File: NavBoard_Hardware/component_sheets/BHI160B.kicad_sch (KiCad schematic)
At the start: 12 parts

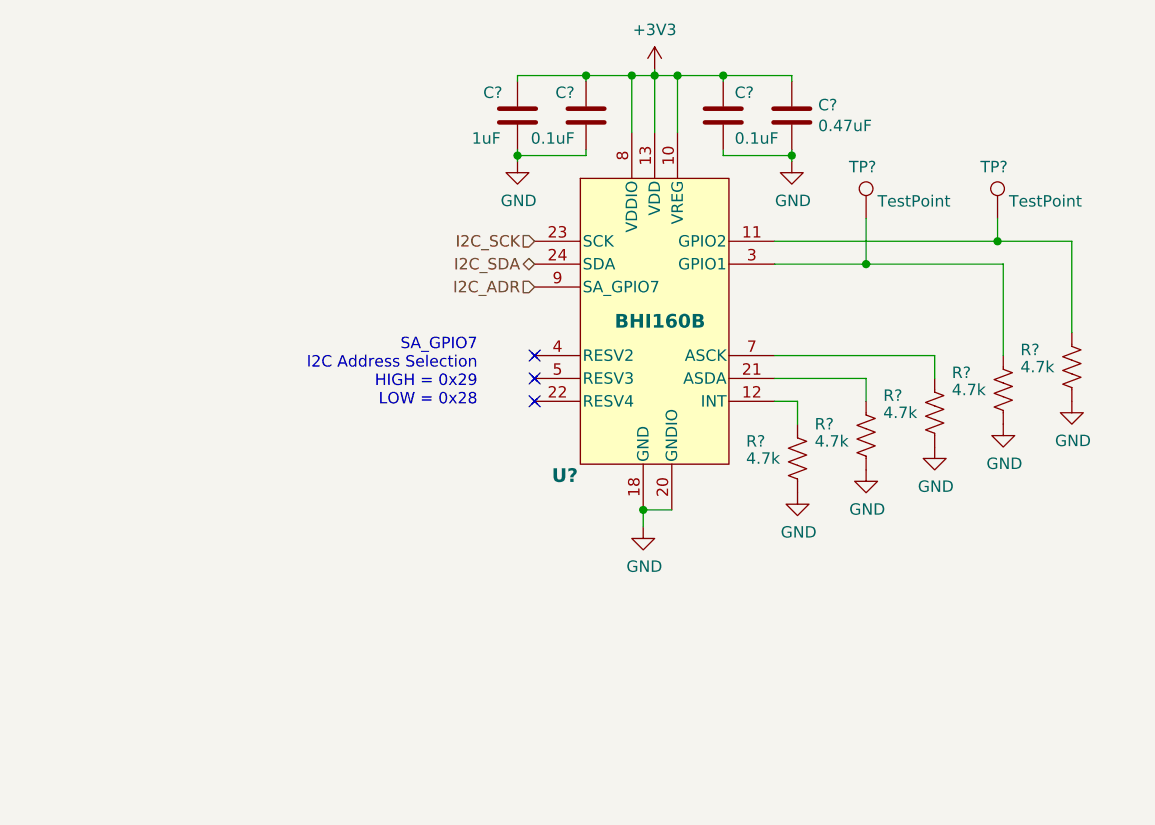
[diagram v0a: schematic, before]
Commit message: Created adapter symbols and footprints
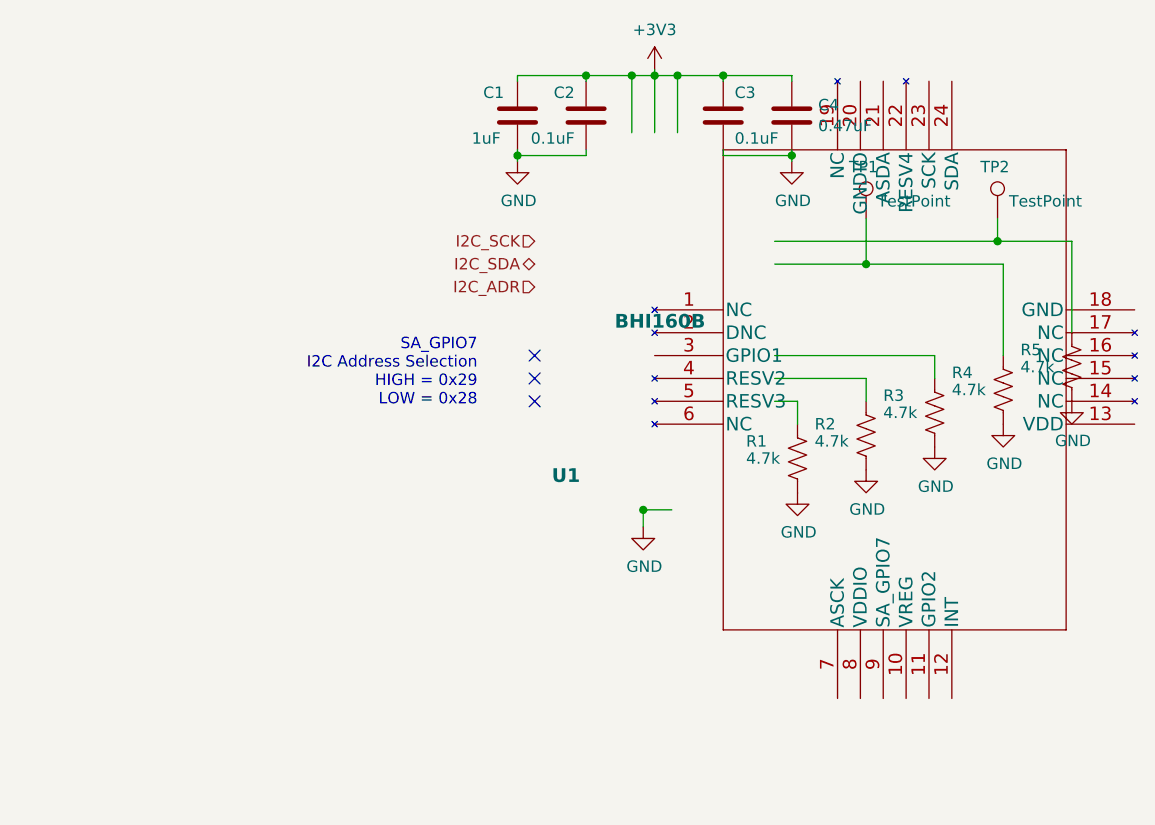
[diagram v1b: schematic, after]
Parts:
- gave numbers to parts that had none: 12
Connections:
- net +3V3: no longer U1.10 (VREG), U1.13 (VDD), U1.8 (VDDIO)
- net GND: no longer U1.18 (GND), U1.20 (GNDIO)
- net I2C_ADR: no longer U1.9 (SA_GPIO7)
- net I2C_SCK: no longer U1.23 (SCK)
- net I2C_SDA: no longer U1.24 (SDA)
- net at R4.1, TP1.1: no longer U1.3 (GPIO1)
- net at R3.1: no longer U1.7 (ASCK)
- net at R5.1, TP2.1: no longer U1.11 (GPIO2)
- net at U1.12 (INT): no longer R1.1
- net at U1.21 (ASDA): no longer R2.1
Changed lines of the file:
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@@
   (symbol (lib_id "Device:R_US") (at 216.535 80.645 0) (unit 1)
     (in_bom yes) (on_board yes)
-    (property "Reference" "R?" (id 0) (at 210.82 78.74 0)
+    (property "Reference" "R4" (id 0) (at 210.82 78.74 0)
       (effects (font (size 1.27 1.27)) (justify left))
     )
@@
   (symbol (lib_id "Device:R_US") (at 208.915 83.185 0) (unit 1)
     (in_bom yes) (on_board yes)
-    (property "Reference" "R?" (id 0) (at 203.2 81.28 0)
+    (property "Reference" "R3" (id 0) (at 203.2 81.28 0)
       (effects (font (size 1.27 1.27)) (justify left))
     )
@@
   (symbol (lib_id "power:GND") (at 176.53 95.885 0) (unit 1)
     (in_bom yes) (on_board yes)
-    (property "Reference" "#PWR?" (id 0) (at 176.53 102.235 0)
+    (property "Reference" "#PWR02" (id 0) (at 176.53 102.235 0)
       (effects (font (size 1.27 1.27)) hide)
     )
@@
   (symbol (lib_id "power:GND") (at 201.295 89.535 0) (unit 1)
     (in_bom yes) (on_board yes)
-    (property "Reference" "#PWR?" (id 0) (at 201.295 95.885 0)
+    (property "Reference" "#PWR06" (id 0) (at 201.295 95.885 0)
       (effects (font (size 1.27 1.27)) hide)
     )
@@
   (symbol (lib_id "Device:R_US") (at 224.155 78.105 0) (unit 1)
     (in_bom yes) (on_board yes)
-    (property "Reference" "R?" (id 0) (at 218.44 76.2 0)
+    (property "Reference" "R5" (id 0) (at 218.44 76.2 0)
       (effects (font (size 1.27 1.27)) (justify left))
     )
@@
   (symbol (lib_id "power:GND") (at 162.56 55.245 0) (unit 1)
     (in_bom yes) (on_board yes)
-    (property "Reference" "#PWR?" (id 0) (at 162.56 61.595 0)
+    (property "Reference" "#PWR01" (id 0) (at 162.56 61.595 0)
       (effects (font (size 1.27 1.27)) hide)
     )
@@
   (symbol (lib_id "power:GND") (at 193.04 55.245 0) (unit 1)
     (in_bom yes) (on_board yes)
-    (property "Reference" "#PWR?" (id 0) (at 193.04 61.595 0)
+    (property "Reference" "#PWR04" (id 0) (at 193.04 61.595 0)
       (effects (font (size 1.27 1.27)) hide)
     )
@@
   (symbol (lib_id "power:GND") (at 216.535 84.455 0) (unit 1)
     (in_bom yes) (on_board yes)
-    (property "Reference" "#PWR?" (id 0) (at 216.535 90.805 0)
+    (property "Reference" "#PWR08" (id 0) (at 216.535 90.805 0)
       (effects (font (size 1.27 1.27)) hide)
     )
@@
   (symbol (lib_id "Device:C") (at 193.04 50.165 0) (unit 1)
     (in_bom yes) (on_board yes)
-    (property "Reference" "C?" (id 0) (at 195.961 48.9966 0)
+    (property "Reference" "C4" (id 0) (at 195.961 48.9966 0)
       (effects (font (size 1.27 1.27)) (justify left))
     )
@@
   (symbol (lib_id "MRDT_Sensors:BHI160B") (at 177.8 71.755 0) (unit 1)
     (in_bom yes) (on_board yes)
-    (property "Reference" "U?" (id 0) (at 166.37 90.17 0)
+    (property "Reference" "U1" (id 0) (at 166.37 90.17 0)
       (effects (font (size 1.524 1.524) bold) (justify left))
     )
@@
       (effects (font (size 1.524 1.524)) hide)
     )
+    (pin "1")
     (pin "10")
     (pin "11")
     (pin "12")
     (pin "13")
+    (pin "14")
+    (pin "15")
+    (pin "16")
+    (pin "17")
     (pin "18")
+    (pin "19")
+    (pin "2")
     (pin "20")
     (pin "21")
@@
     (pin "4")
     (pin "5")
+    (pin "6")
     (pin "7")
     (pin "8")
@@
   (symbol (lib_id "Device:R_US") (at 193.675 88.265 0) (unit 1)
     (in_bom yes) (on_board yes)
-    (property "Reference" "R?" (id 0) (at 187.96 86.36 0)
+    (property "Reference" "R1" (id 0) (at 187.96 86.36 0)
       (effects (font (size 1.27 1.27)) (justify left))
     )
@@
   (symbol (lib_id "power:+3V3") (at 177.8 45.085 0) (unit 1)
     (in_bom yes) (on_board yes)
-    (property "Reference" "#PWR?" (id 0) (at 177.8 48.895 0)
+    (property "Reference" "#PWR03" (id 0) (at 177.8 48.895 0)
       (effects (font (size 1.27 1.27)) hide)
     )
@@
   (symbol (lib_id "Connector:TestPoint") (at 215.9 61.595 0) (unit 1)
     (in_bom yes) (on_board yes)
-    (property "Reference" "TP?" (id 0) (at 213.995 55.88 0)
+    (property "Reference" "TP2" (id 0) (at 213.995 55.88 0)
       (effects (font (size 1.27 1.27)) (justify left))
     )
@@
   (symbol (lib_id "power:GND") (at 224.155 81.915 0) (unit 1)
     (in_bom yes) (on_board yes)
-    (property "Reference" "#PWR?" (id 0) (at 224.155 88.265 0)
+    (property "Reference" "#PWR09" (id 0) (at 224.155 88.265 0)
       (effects (font (size 1.27 1.27)) hide)
     )
@@
   (symbol (lib_id "Device:C") (at 170.18 50.165 0) (mirror y) (unit 1)
     (in_bom yes) (on_board yes)
-    (property "Reference" "C?" (id 0) (at 168.91 47.625 0)
+    (property "Reference" "C2" (id 0) (at 168.91 47.625 0)
       (effects (font (size 1.27 1.27)) (justify left))
     )
@@
   (symbol (lib_id "power:GND") (at 208.915 86.995 0) (unit 1)
     (in_bom yes) (on_board yes)
-    (property "Reference" "#PWR?" (id 0) (at 208.915 93.345 0)
+    (property "Reference" "#PWR07" (id 0) (at 208.915 93.345 0)
       (effects (font (size 1.27 1.27)) hide)
     )
@@
   (symbol (lib_id "Device:C") (at 185.42 50.165 0) (unit 1)
     (in_bom yes) (on_board yes)
-    (property "Reference" "C?" (id 0) (at 186.69 47.625 0)
+    (property "Reference" "C3" (id 0) (at 186.69 47.625 0)
       (effects (font (size 1.27 1.27)) (justify left))
     )
@@
   (symbol (lib_id "Device:R_US") (at 201.295 85.725 0) (unit 1)
     (in_bom yes) (on_board yes)
-    (property "Reference" "R?" (id 0) (at 195.58 84.455 0)
+    (property "Reference" "R2" (id 0) (at 195.58 84.455 0)
       (effects (font (size 1.27 1.27)) (justify left))
     )
@@
   (symbol (lib_id "Device:C") (at 162.56 50.165 0) (unit 1)
     (in_bom yes) (on_board yes)
-    (property "Reference" "C?" (id 0) (at 158.75 47.625 0)
+    (property "Reference" "C1" (id 0) (at 158.75 47.625 0)
       (effects (font (size 1.27 1.27)) (justify left))
     )
@@
   (symbol (lib_id "power:GND") (at 193.675 92.075 0) (unit 1)
     (in_bom yes) (on_board yes)
-    (property "Reference" "#PWR?" (id 0) (at 193.675 98.425 0)
+    (property "Reference" "#PWR05" (id 0) (at 193.675 98.425 0)
       (effects (font (size 1.27 1.27)) hide)
     )
@@
   (symbol (lib_id "Connector:TestPoint") (at 201.295 61.595 0) (unit 1)
     (in_bom yes) (on_board yes)
-    (property "Reference" "TP?" (id 0) (at 199.39 55.88 0)
-      (effects (font (size 1.27 1.27)) (justify left))
-    )
+    (property "Reference" "TP1" (id 0) (at 199.39 55.88 0)
+      (effects (font (size 1.27 1.27)) (justify left))
+    )

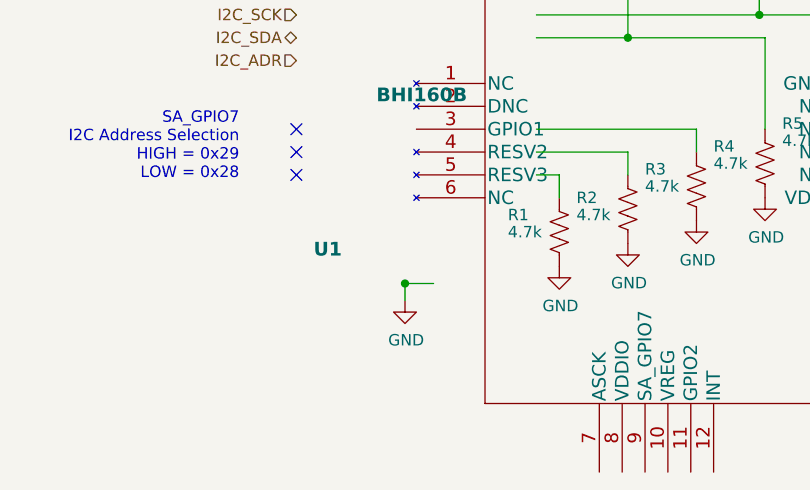
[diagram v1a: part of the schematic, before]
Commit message: Added connectors, cleaned up file directory
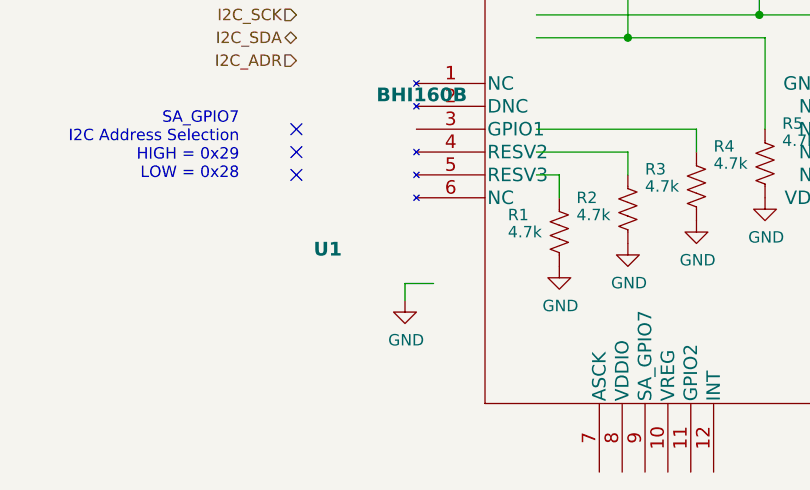
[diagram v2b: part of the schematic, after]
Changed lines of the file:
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@@
   (junction (at 162.56 54.61) (diameter 0) (color 0 0 0 0)
-  )
-  (junction (at 176.53 93.98) (diameter 0) (color 0 0 0 0)
   )
   (junction (at 170.18 45.72) (diameter 0) (color 0 0 0 0)

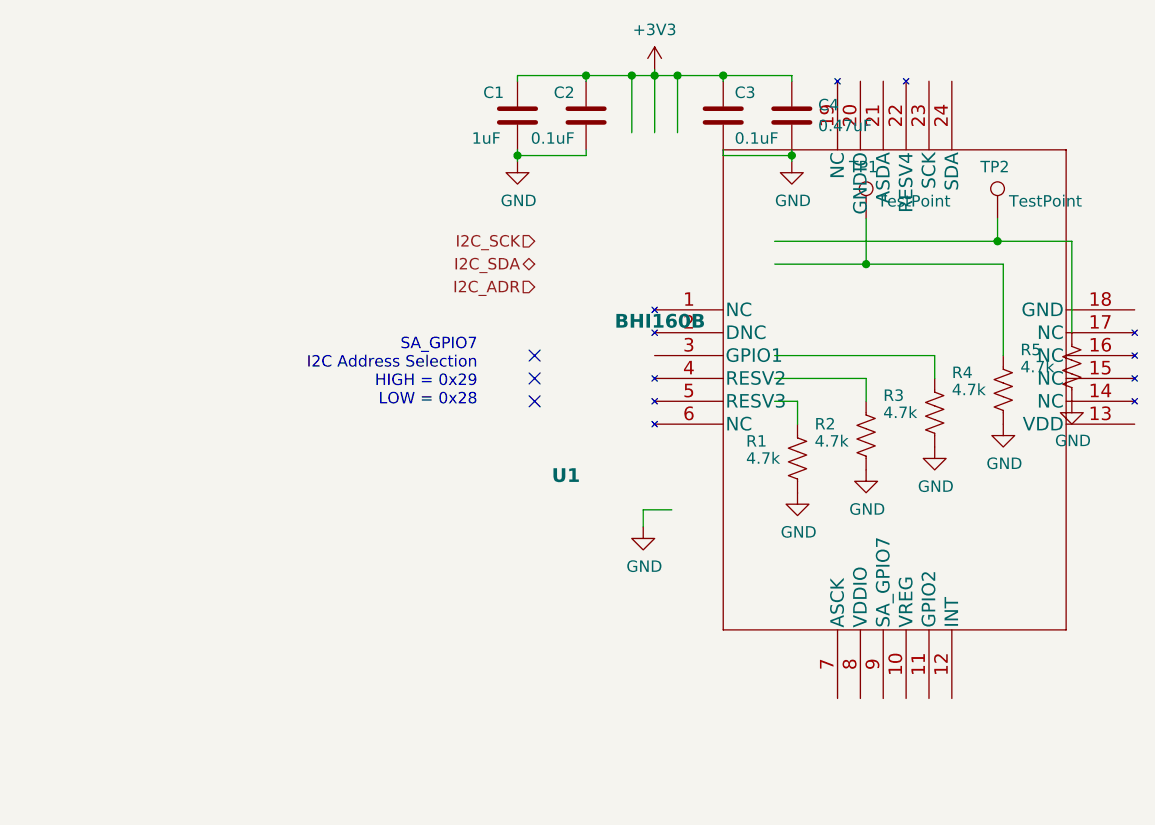
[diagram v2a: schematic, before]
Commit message: Updated BMI component sheet from Navboard_2023_rev2
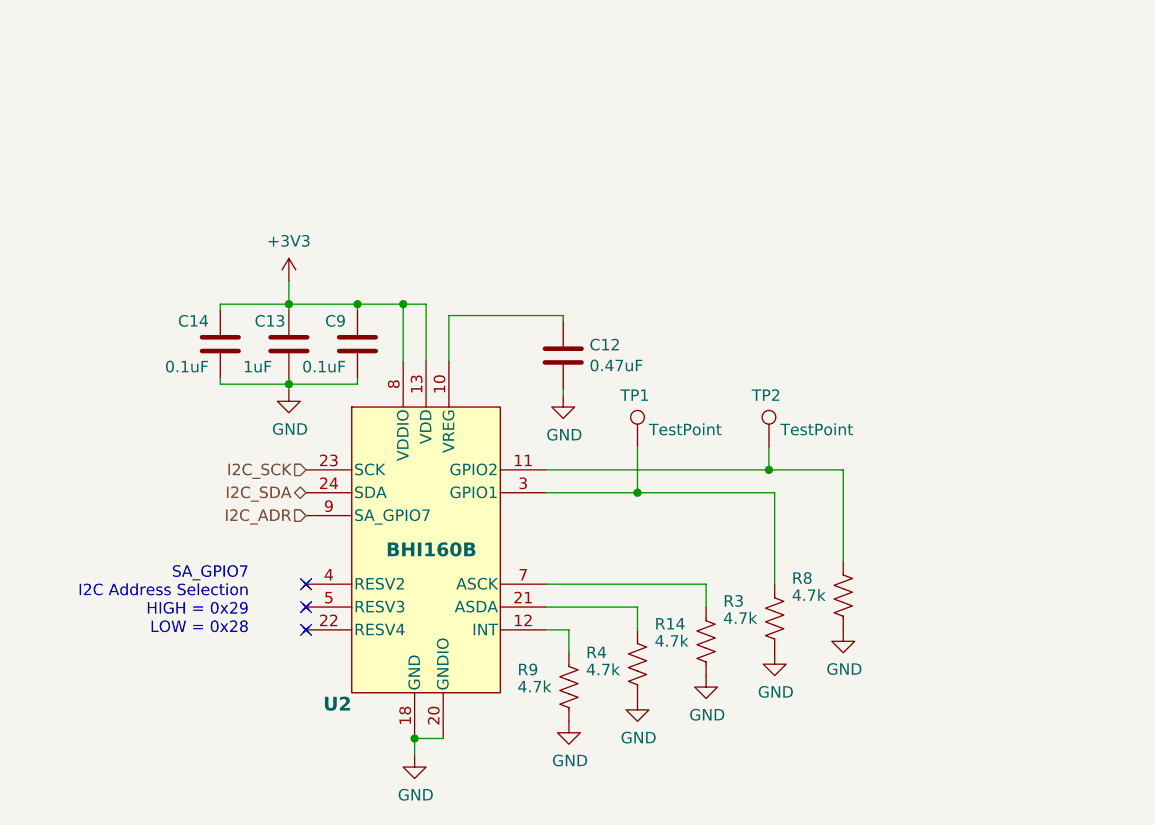
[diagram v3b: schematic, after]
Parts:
- renumbered C4 to C12, C1 to C13, C3 to C14, C2 to C9, R3 to R14, R4 to R3, R2 to R4, R5 to R8, R1 to R9, U1 to U2
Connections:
- net +3V3: now also U2.13 (VDD), U2.8 (VDDIO); no longer C12.1
- net GND: now also U2.18 (GND), U2.20 (GNDIO)
- net I2C_ADR: now also U2.9 (SA_GPIO7)
- net I2C_SCK: now also U2.23 (SCK)
- net I2C_SDA: now also U2.24 (SDA)
- net at R3.1, TP1.1: now also U2.3 (GPIO1)
- net at R14.1: now also U2.7 (ASCK)
- net at R8.1, TP2.1: now also U2.11 (GPIO2)
- net at U2.10 (VREG): now also C12.1
- net at U2.12 (INT): now also R9.1
- net at U2.21 (ASDA): now also R4.1
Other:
- company: Missouri S&T Rover Design Team -> Thomas Francois, Katherine Dunlap, Missouri S&T Mars Rover Design Team
- moved on the sheet: C12, C13, C14, C9, R14, R3, R4, R8, R9, TP1, TP2
